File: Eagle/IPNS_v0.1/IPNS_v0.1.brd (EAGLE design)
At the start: 100 x 80 mm, 1 part, among them U1 STM8L152C4_C6TX

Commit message: Powering up microcontroller
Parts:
- added C1, C5, C6, C7, C8, C9: 1u, IPNS_Lib_v0.1:C0805
- added C2, C3: 20pF, IPNS_Lib_v0.1:C0805
- added C4: 100n, IPNS_Lib_v0.1:C0805
- added J1: (no value), IPNS_Lib_v0.1:1X04
- added Q1: 16MHz, IPNS_Lib_v0.1:HC49/S
- added R1: 0, IPNS_Lib_v0.1:R0805
- added U$1, U$2: PUSH-BUTTON, IPNS_Lib_v0.1:PUSH-BUTTON
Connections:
- removed net VDD: U1.10
- removed net VDD2: U1.39
- removed net VLCD: U1.13
- removed net VREF+: U1.12
- removed net VSS1/VSSA/VREF-: U1.9
- removed net VSS2: U1.40
- new net +3V3: C1.1, C5.1, C6.1, C7.1, J1.1, U$2.1, U1.10, U1.13, U1.39
- new net GND: C1.2, C2.1, C3.1, C4.2, C5.2, C6.2, C7.2, C8.2, C9.2, J1.3, U$1.1, U1.40, U1.9
- new net N$1: C2.2, Q1.2, U1.3
- new net N$2: R1.2, U1.4
- new net N$5: C3.2, Q1.1, R1.1
- new net RESET: C4.1, J1.4, U$1.3, U1.2
- new net ST_LINK_SWIM: J1.2, U1.1
- net VDDA: now also C8.1, C9.1, U$2.3, U1.12
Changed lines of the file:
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@@
 <attribute name="COPYRIGHT" value="Copyright (C) 2016 Accelerated Designs. All rights reserved" x="-25.4" y="6.35" size="1.778" layer="27" display="off"/>
 </element>
+<element name="C1" library="IPNS_Lib_v0.1" package="C0805" value="1u" x="-29.21" y="-3.81"/>
+<element name="Q1" library="IPNS_Lib_v0.1" package="HC49/S" value="16MHz" x="-22.86" y="-13.97">
+<attribute name="MF" value="" x="-22.86" y="-13.97" size="1.778" layer="27" display="off"/>
+<attribute name="OC_FARNELL" value="1667008" x="-22.86" y="-13.97" size="1.778" layer="27" display="off"/>
+<attribute name="OC_NEWARK" value="unknown" x="-22.86" y="-13.97" size="1.778" layer="27" display="off"/>
+<attribute name="MPN" value="" x="-22.86" y="-13.97" size="1.778" layer="27" display="off"/>
+</element>
+<element name="C2" library="IPNS_Lib_v0.1" package="C0805" value="20pF" x="-29.21" y="-24.13"/>
+<element name="C3" library="IPNS_Lib_v0.1" package="C0805" value="20pF" x="-29.21" y="-30.48"/>
+<element name="R1" library="IPNS_Lib_v0.1" package="R0805" value="0" x="-29.21" y="-36.83"/>
+<element name="J1" library="IPNS_Lib_v0.1" package="1X04" value="" x="-21.59" y="-49.53">
+<attribute name="PROD_ID" value="CONN-09696" x="-21.59" y="-49.53" size="1.778" layer="27" display="off"/>
+</element>
+<element name="U$1" library="IPNS_Lib_v0.1" package="PUSH-BUTTON" value="PUSH-BUTTON" x="-19.05" y="-68.58"/>
+<element name="C4" library="IPNS_Lib_v0.1" package="C0805" value="100n" x="-29.21" y="-81.28"/>
+<element name="C5" library="IPNS_Lib_v0.1" package="C0805" value="1u" x="-29.21" y="-87.63"/>
+<element name="C6" library="IPNS_Lib_v0.1" package="C0805" value="1u" x="-29.21" y="-93.98"/>
+<element name="C7" library="IPNS_Lib_v0.1" package="C0805" value="1u" x="-29.21" y="-100.33"/>
+<element name="C8" library="IPNS_Lib_v0.1" package="C0805" value="1u" x="-29.21" y="-106.68"/>
+<element name="C9" library="IPNS_Lib_v0.1" package="C0805" value="1u" x="-29.21" y="-113.03"/>
+<element name="U$2" library="IPNS_Lib_v0.1" package="PUSH-BUTTON" value="PUSH-BUTTON" x="-19.05" y="-125.73"/>
 </elements>
 <signals>
-<signal name="VLCD">
+<signal name="+3V3">
+<contactref element="C1" pad="1"/>
+<contactref element="U1" pad="39"/>
+<contactref element="U1" pad="10"/>
 <contactref element="U1" pad="13"/>
+<contactref element="C7" pad="1"/>
+<contactref element="C6" pad="1"/>
+<contactref element="C5" pad="1"/>
+<contactref element="J1" pad="1"/>
+<contactref element="U$2" pad="1"/>
+<wire x1="-30.16" y1="-100.33" x2="-21.59" y2="-125.73" width="0" layer="19" extent="1-1"/>
+<wire x1="-30.16" y1="-93.98" x2="-30.16" y2="-100.33" width="0" layer="19" extent="1-1"/>
+<wire x1="-30.16" y1="-87.63" x2="-30.16" y2="-93.98" width="0" layer="19" extent="1-1"/>
+<wire x1="-21.59" y1="-49.53" x2="-30.16" y2="-87.63" width="0" layer="19" extent="1-1"/>
+<wire x1="-30.16" y1="-3.81" x2="-21.59" y2="-49.53" width="0" layer="19" extent="1-1"/>
+<wire x1="-28.15000625" y1="2.1336" x2="-30.16" y2="-3.81" width="0" layer="19" extent="1-1"/>
+<wire x1="-29.6164" y1="4.599990625" x2="-28.15000625" y2="2.1336" width="0" layer="19" extent="1-1"/>
+<wire x1="-23.649990625" y1="10.5664" x2="-29.6164" y2="4.599990625" width="0" layer="19" extent="1-1"/>
 </signal>
-<signal name="VSS1/VSSA/VREF-">
+<signal name="GND">
 <contactref element="U1" pad="9"/>
+<contactref element="U1" pad="40"/>
+<contactref element="C1" pad="2"/>
+<contactref element="C2" pad="1"/>
+<contactref element="C3" pad="1"/>
+<contactref element="U$1" pad="1"/>
+<contactref element="C4" pad="2"/>
+<contactref element="C5" pad="2"/>
+<contactref element="C6" pad="2"/>
+<contactref element="C7" pad="2"/>
+<contactref element="C8" pad="2"/>
+<contactref element="C9" pad="2"/>
+<contactref element="J1" pad="3"/>
+<wire x1="-28.26" y1="-106.68" x2="-28.26" y2="-113.03" width="0" layer="19" extent="1-1"/>
+<wire x1="-28.26" y1="-100.33" x2="-28.26" y2="-106.68" width="0" layer="19" extent="1-1"/>
+<wire x1="-28.26" y1="-93.98" x2="-28.26" y2="-100.33" width="0" layer="19" extent="1-1"/>
+<wire x1="-28.26" y1="-87.63" x2="-28.26" y2="-93.98" width="0" layer="19" extent="1-1"/>
+<wire x1="-28.26" y1="-81.28" x2="-28.26" y2="-87.63" width="0" layer="19" extent="1-1"/>
+<wire x1="-21.59" y1="-68.58" x2="-28.26" y2="-81.28" width="0" layer="19" extent="1-1"/>
+<wire x1="-16.51" y1="-49.53" x2="-21.59" y2="-68.58" width="0" layer="19" extent="1-1"/>
+<wire x1="-30.16" y1="-30.48" x2="-16.51" y2="-49.53" width="0" layer="19" extent="1-1"/>
+<wire x1="-30.16" y1="-24.13" x2="-30.16" y2="-30.48" width="0" layer="19" extent="1-1"/>
+<wire x1="-28.26" y1="-3.81" x2="-30.16" y2="-24.13" width="0" layer="19" extent="1-1"/>
+<wire x1="-29.6164" y1="5.099990625" x2="-28.26" y2="-3.81" width="0" layer="19" extent="1-1"/>
+<wire x1="-24.149990625" y1="10.5664" x2="-29.6164" y2="5.099990625" width="0" layer="19" extent="1-1"/>
 </signal>
-<signal name="VSS2">
-<contactref element="U1" pad="40"/>
+<signal name="N$1">
+<contactref element="C2" pad="2"/>
+<contactref element="Q1" pad="2"/>
+<contactref element="U1" pad="3"/>
+<wire x1="-20.447" y1="-13.97" x2="-28.26" y2="-24.13" width="0" layer="19" extent="1-1"/>
+<wire x1="-29.6164" y1="8.100009375" x2="-20.447" y2="-13.97" width="0" layer="19" extent="1-1"/>
 </signal>
-<signal name="VREF+">
-<contactref element="U1" pad="12"/>
+<signal name="N$2">
+<contactref element="U1" pad="4"/>
+<contactref element="R1" pad="2"/>
+<wire x1="-29.6164" y1="7.600009375" x2="-28.26" y2="-36.83" width="0" layer="19" extent="1-1"/>
+</signal>
+<signal name="N$5">
+<contactref element="C3" pad="2"/>
+<contactref element="Q1" pad="1"/>
+<contactref element="R1" pad="1"/>
+<wire x1="-28.26" y1="-30.48" x2="-30.16" y2="-36.83" width="0" layer="19" extent="1-1"/>
+<wire x1="-25.273" y1="-13.97" x2="-28.26" y2="-30.48" width="0" layer="19" extent="1-1"/>
+</signal>
+<signal name="RESET">
+<contactref element="U$1" pad="3"/>
+<contactref element="C4" pad="1"/>
+<contactref element="U1" pad="2"/>
+<contactref element="J1" pad="4"/>
+<wire x1="-16.51" y1="-68.58" x2="-30.16" y2="-81.28" width="0" layer="19" extent="1-1"/>
+<wire x1="-13.97" y1="-49.53" x2="-16.51" y2="-68.58" width="0" layer="19" extent="1-1"/>
+<wire x1="-29.6164" y1="8.600009375" x2="-13.97" y2="-49.53" width="0" layer="19" extent="1-1"/>
+</signal>
+<signal name="ST_LINK_SWIM">
+<contactref element="U1" pad="1"/>
+<contactref element="J1" pad="2"/>
+<wire x1="-29.6164" y1="9.10000625" x2="-19.05" y2="-49.53" width="0" layer="19" extent="1-1"/>
 </signal>
 <signal name="VDDA">
+<contactref element="C8" pad="1"/>
+<contactref element="C9" pad="1"/>
 <contactref element="U1" pad="11"/>
-</signal>
-<signal name="VDD">
-<contactref element="U1" pad="10"/>
-</signal>
-<signal name="VDD2">
-<contactref element="U1" pad="39"/>
+<contactref element="U1" pad="12"/>
+<contactref element="U$2" pad="3"/>
+<wire x1="-30.16" y1="-106.68" x2="-30.16" y2="-113.03" width="0" layer="19" extent="1-1"/>
+<wire x1="-16.51" y1="-125.73" x2="-30.16" y2="-113.03" width="0" layer="19" extent="1-1"/>
+<wire x1="-29.6164" y1="3.59999375" x2="-30.16" y2="-106.68" width="0" layer="19" extent="1-1"/>
+<wire x1="-29.6164" y1="4.099990625" x2="-29.6164" y2="3.59999375" width="0" layer="19" extent="1-1"/>
 </signal>
 </signals>

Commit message: Microcontroller setup possibly finished with minor unknowns
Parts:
- added C10, C11: 7pF, IPNS_Lib_v0.1:C0805
- added C12: (no value), IPNS_Lib_v0.1:C0805
- added J2: (no value), IPNS_Lib_v0.1:1X04
- added LED1: RED, led:CHIP-LED0805
- added LED2: GREEN, led:CHIP-LED0805
- added LED3: BLUE, led:CHIP-LED0805
- added Q2: 32.768 kHz, IPNS_Lib_v0.1:TC26H
- added R2: 0, IPNS_Lib_v0.1:R0805
- added R3, R4, R5, R6, R7: (no value), IPNS_Lib_v0.1:R0805
- C6, C7, C9: value 1u -> 100n
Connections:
- new net DAC: U1.32
- new net N$11: LED1.A, R3.1
- new net N$12: LED2.A, R4.1
- new net N$13: LED3.A, R5.1
- new net N$14: R3.2, U1.48
- new net N$15: R4.2, U1.47
- new net N$16: R5.2, U1.19
- new net N$3: C11.2, Q2.1, R2.1
- new net N$4: C5.1, C6.1, C7.1, U$2.1
- new net N$6: C10.2, Q2.2, U1.44
- new net N$8: R2.2, U1.45
- new net PULSE: U1.22
- new net SCL: J2.3, R6.1, U1.38
- new net SDA: J2.4, R7.1, U1.37
- net +3V3: now also C12.2, J2.2, R6.2, R7.2; no longer C5.1, C6.1, C7.1, U$2.1
- net GND: now also C10.1, C11.1, C12.1, J2.1, LED1.C, LED2.C, LED3.C
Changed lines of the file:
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@@
 <setting verticaltext="up"/>
 </settings>
-<grid distance="0.05" unitdist="inch" unit="inch" style="lines" multiple="1" display="no" altdistance="0.025" altunitdist="inch" altunit="inch"/>
+<grid distance="0.05" unitdist="inch" unit="inch" style="lines" multiple="1" display="yes" altdistance="0.025" altunitdist="inch" altunit="inch"/>
 <layers>
 <layer number="1" name="Top" color="4" fill="1" visible="yes" active="yes"/>
@@
 <element name="C4" library="IPNS_Lib_v0.1" package="C0805" value="100n" x="-29.21" y="-81.28"/>
 <element name="C5" library="IPNS_Lib_v0.1" package="C0805" value="1u" x="-29.21" y="-87.63"/>
-<element name="C6" library="IPNS_Lib_v0.1" package="C0805" value="1u" x="-29.21" y="-93.98"/>
-<element name="C7" library="IPNS_Lib_v0.1" package="C0805" value="1u" x="-29.21" y="-100.33"/>
+<element name="C6" library="IPNS_Lib_v0.1" package="C0805" value="100n" x="-29.21" y="-93.98"/>
+<element name="C7" library="IPNS_Lib_v0.1" package="C0805" value="100n" x="-29.21" y="-100.33"/>
 <element name="C8" library="IPNS_Lib_v0.1" package="C0805" value="1u" x="-29.21" y="-106.68"/>
-<element name="C9" library="IPNS_Lib_v0.1" package="C0805" value="1u" x="-29.21" y="-113.03"/>
+<element name="C9" library="IPNS_Lib_v0.1" package="C0805" value="100n" x="-29.21" y="-113.03"/>
 <element name="U$2" library="IPNS_Lib_v0.1" package="PUSH-BUTTON" value="PUSH-BUTTON" x="-19.05" y="-125.73"/>
+<element name="Q2" library="IPNS_Lib_v0.1" package="TC26H" value="32.768 kHz" x="-21.59" y="-144.78">
+<attribute name="MF" value="" x="-21.59" y="-144.78" size="1.778" layer="27" display="off"/>
+<attribute name="OC_FARNELL" value="unknown" x="-21.59" y="-144.78" size="1.778" layer="27" display="off"/>
+<attribute name="OC_NEWARK" value="unknown" x="-21.59" y="-144.78" size="1.778" layer="27" display="off"/>
+<attribute name="MPN" value="" x="-21.59" y="-144.78" size="1.778" layer="27" display="off"/>
+</element>
+<element name="C10" library="IPNS_Lib_v0.1" package="C0805" value="7pF" x="-29.21" y="-156.21"/>
+<element name="C11" library="IPNS_Lib_v0.1" package="C0805" value="7pF" x="-29.21" y="-162.56"/>
+<element name="R2" library="IPNS_Lib_v0.1" package="R0805" value="0" x="-29.21" y="-168.91"/>
+<element name="R3" library="IPNS_Lib_v0.1" package="R0805" value="" x="-29.21" y="-175.26"/>
+<element name="R4" library="IPNS_Lib_v0.1" package="R0805" value="" x="-29.21" y="-181.61"/>
+<element name="R5" library="IPNS_Lib_v0.1" package="R0805" value="" x="-29.21" y="-187.96"/>
+<element name="LED1" library="led" package="CHIP-LED0805" value="RED" x="-35.56" y="-187.96"/>
+<element name="LED2" library="led" package="CHIP-LED0805" value="GREEN" x="-41.91" y="-187.96"/>
+<element name="LED3" library="led" package="CHIP-LED0805" value="BLUE" x="-48.26" y="-187.96"/>
+<element name="J2" library="IPNS_Lib_v0.1" package="1X04" value="" x="-40.64" y="-200.66">
+<attribute name="PROD_ID" value="CONN-09696" x="-40.64" y="-200.66" size="1.778" layer="27" display="off"/>
+</element>
+<element name="C12" library="IPNS_Lib_v0.1" package="C0805" value="" x="-48.26" y="-213.36"/>
+<element name="R6" library="IPNS_Lib_v0.1" package="R0805" value="" x="-48.26" y="-219.71"/>
+<element name="R7" library="IPNS_Lib_v0.1" package="R0805" value="" x="-48.26" y="-226.06"/>
 </elements>
 <signals>
@@
 <contactref element="U1" pad="10"/>
 <contactref element="U1" pad="13"/>
-<contactref element="C7" pad="1"/>
-<contactref element="C6" pad="1"/>
-<contactref element="C5" pad="1"/>
 <contactref element="J1" pad="1"/>
-<contactref element="U$2" pad="1"/>
-<wire x1="-30.16" y1="-100.33" x2="-21.59" y2="-125.73" width="0" layer="19" extent="1-1"/>
-<wire x1="-30.16" y1="-93.98" x2="-30.16" y2="-100.33" width="0" layer="19" extent="1-1"/>
-<wire x1="-30.16" y1="-87.63" x2="-30.16" y2="-93.98" width="0" layer="19" extent="1-1"/>
-<wire x1="-21.59" y1="-49.53" x2="-30.16" y2="-87.63" width="0" layer="19" extent="1-1"/>
+<contactref element="J2" pad="2"/>
+<contactref element="C12" pad="2"/>
+<contactref element="R6" pad="2"/>
+<contactref element="R7" pad="2"/>
+<wire x1="-47.31" y1="-213.36" x2="-38.1" y2="-200.66" width="0" layer="19" extent="1-1"/>
+<wire x1="-47.31" y1="-219.71" x2="-47.31" y2="-213.36" width="0" layer="19" extent="1-1"/>
+<wire x1="-47.31" y1="-226.06" x2="-47.31" y2="-219.71" width="0" layer="19" extent="1-1"/>
+<wire x1="-21.59" y1="-49.53" x2="-38.1" y2="-200.66" width="0" layer="19" extent="1-1"/>
 <wire x1="-30.16" y1="-3.81" x2="-21.59" y2="-49.53" width="0" layer="19" extent="1-1"/>
 <wire x1="-28.15000625" y1="2.1336" x2="-30.16" y2="-3.81" width="0" layer="19" extent="1-1"/>
@@
 <contactref element="C9" pad="2"/>
 <contactref element="J1" pad="3"/>
+<contactref element="C10" pad="1"/>
+<contactref element="C11" pad="1"/>
+<contactref element="LED1" pad="C"/>
+<contactref element="LED2" pad="C"/>
+<contactref element="LED3" pad="C"/>
+<contactref element="J2" pad="1"/>
+<contactref element="C12" pad="1"/>
+<wire x1="-41.91" y1="-186.91" x2="-40.64" y2="-200.66" width="0" layer="19" extent="1-1"/>
+<wire x1="-48.26" y1="-186.91" x2="-41.91" y2="-186.91" width="0" layer="19" extent="1-1"/>
+<wire x1="-35.56" y1="-186.91" x2="-41.91" y2="-186.91" width="0" layer="19" extent="1-1"/>
+<wire x1="-49.21" y1="-213.36" x2="-40.64" y2="-200.66" width="0" layer="19" extent="1-1"/>
+<wire x1="-30.16" y1="-162.56" x2="-35.56" y2="-186.91" width="0" layer="19" extent="1-1"/>
+<wire x1="-30.16" y1="-156.21" x2="-30.16" y2="-162.56" width="0" layer="19" extent="1-1"/>
+<wire x1="-28.26" y1="-113.03" x2="-30.16" y2="-156.21" width="0" layer="19" extent="1-1"/>
 <wire x1="-28.26" y1="-106.68" x2="-28.26" y2="-113.03" width="0" layer="19" extent="1-1"/>
 <wire x1="-28.26" y1="-100.33" x2="-28.26" y2="-106.68" width="0" layer="19" extent="1-1"/>
@@
 <wire x1="-29.6164" y1="4.099990625" x2="-29.6164" y2="3.59999375" width="0" layer="19" extent="1-1"/>
 </signal>
+<signal name="N$4">
+<contactref element="C5" pad="1"/>
+<contactref element="C6" pad="1"/>
+<contactref element="C7" pad="1"/>
+<contactref element="U$2" pad="1"/>
+<wire x1="-30.16" y1="-100.33" x2="-21.59" y2="-125.73" width="0" layer="19" extent="1-1"/>
+<wire x1="-30.16" y1="-93.98" x2="-30.16" y2="-100.33" width="0" layer="19" extent="1-1"/>
+<wire x1="-30.16" y1="-87.63" x2="-30.16" y2="-93.98" width="0" layer="19" extent="1-1"/>
+</signal>
+<signal name="N$3">
+<contactref element="R2" pad="1"/>
+<contactref element="C11" pad="2"/>
+<contactref element="Q2" pad="1"/>
+<wire x1="-28.26" y1="-162.56" x2="-30.16" y2="-168.91" width="0" layer="19" extent="1-1"/>
+<wire x1="-22.86" y1="-144.78" x2="-28.26" y2="-162.56" width="0" layer="19" extent="1-1"/>
+</signal>
+<signal name="N$6">
+<contactref element="Q2" pad="2"/>
+<contactref element="C10" pad="2"/>
+<contactref element="U1" pad="44"/>
+<wire x1="-20.32" y1="-144.78" x2="-28.26" y2="-156.21" width="0" layer="19" extent="1-1"/>
+<wire x1="-26.1500125" y1="10.5664" x2="-20.32" y2="-144.78" width="0" layer="19" extent="1-1"/>
+</signal>
+<signal name="N$8">
+<contactref element="U1" pad="45"/>
+<contactref element="R2" pad="2"/>
+<wire x1="-26.650009375" y1="10.5664" x2="-28.26" y2="-168.91" width="0" layer="19" extent="1-1"/>
+</signal>
+<signal name="N$11">
+<contactref element="LED1" pad="A"/>
+<contactref element="R3" pad="1"/>
+<wire x1="-30.16" y1="-175.26" x2="-35.56" y2="-189.01" width="0" layer="19" extent="1-1"/>
+</signal>
+<signal name="N$12">
+<contactref element="LED2" pad="A"/>
+<contactref element="R4" pad="1"/>
+<wire x1="-30.16" y1="-181.61" x2="-41.91" y2="-189.01" width="0" layer="19" extent="1-1"/>
+</signal>
+<signal name="N$13">
+<contactref element="LED3" pad="A"/>
+<contactref element="R5" pad="1"/>
+<wire x1="-30.16" y1="-187.96" x2="-48.26" y2="-189.01" width="0" layer="19" extent="1-1"/>
+</signal>
+<signal name="N$14">
+<contactref element="R3" pad="2"/>
+<contactref element="U1" pad="48"/>
+<wire x1="-28.15000625" y1="10.5664" x2="-28.26" y2="-175.26" width="0" layer="19" extent="1-1"/>
+</signal>
+<signal name="N$15">
+<contactref element="R4" pad="2"/>
+<contactref element="U1" pad="47"/>
+<wire x1="-27.650009375" y1="10.5664" x2="-28.26" y2="-181.61" width="0" layer="19" extent="1-1"/>
+</signal>
+<signal name="N$16">
+<contactref element="R5" pad="2"/>
+<contactref element="U1" pad="19"/>
+<wire x1="-25.1500125" y1="2.1336" x2="-28.26" y2="-187.96" width="0" layer="19" extent="1-1"/>
+</signal>
+<signal name="DAC">
+<contactref element="U1" pad="32"/>
+</signal>
+<signal name="PULSE">
+<contactref element="U1" pad="22"/>
+</signal>
+<signal name="SCL">
+<contactref element="U1" pad="38"/>
+<contactref element="J2" pad="3"/>
+<contactref element="R6" pad="1"/>
+<wire x1="-49.21" y1="-219.71" x2="-35.56" y2="-200.66" width="0" layer="19" extent="1-1"/>
+<wire x1="-23.149990625" y1="10.5664" x2="-35.56" y2="-200.66" width="0" layer="19" extent="1-1"/>
+</signal>
+<signal name="SDA">
+<contactref element="U1" pad="37"/>
+<contactref element="J2" pad="4"/>
+<contactref element="R7" pad="1"/>
+<wire x1="-49.21" y1="-226.06" x2="-33.02" y2="-200.66" width="0" layer="19" extent="1-1"/>
+<wire x1="-22.64999375" y1="10.5664" x2="-33.02" y2="-200.66" width="0" layer="19" extent="1-1"/>
+</signal>
 </signals>

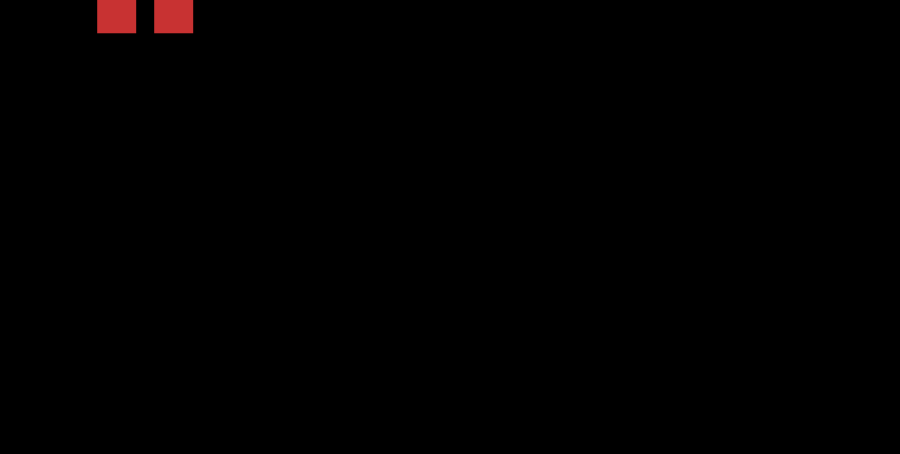
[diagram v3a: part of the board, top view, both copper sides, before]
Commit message: Various connectors implemented: SWIM , battery supply board, and NFC memory connector
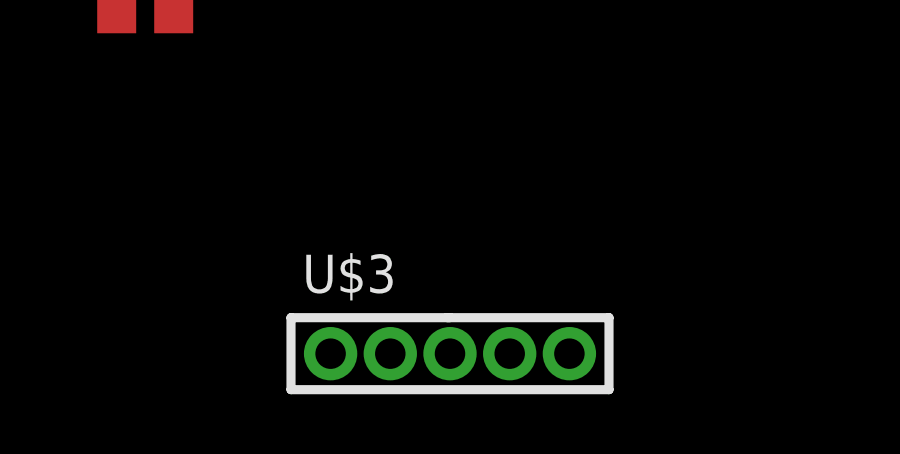
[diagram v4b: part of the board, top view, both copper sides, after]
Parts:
- added U$3: SLIDE_SWITCH, IPNS_Lib_v0.1:SLIDE_SWITCH
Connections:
- new net OFF: U$3.2
- new net VBATT: U$3.3
- net +3V3: now also U$3.4
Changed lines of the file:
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@@
 <element name="R6" library="IPNS_Lib_v0.1" package="R0805" value="" x="-48.26" y="-219.71"/>
 <element name="R7" library="IPNS_Lib_v0.1" package="R0805" value="" x="-48.26" y="-226.06"/>
+<element name="U$3" library="IPNS_Lib_v0.1" package="SLIDE_SWITCH" value="SLIDE_SWITCH" x="-38.1" y="-237.49"/>
 </elements>
 <signals>
@@
 <contactref element="R6" pad="2"/>
 <contactref element="R7" pad="2"/>
+<contactref element="U$3" pad="4"/>
 <wire x1="-47.31" y1="-213.36" x2="-38.1" y2="-200.66" width="0" layer="19" extent="1-1"/>
 <wire x1="-47.31" y1="-219.71" x2="-47.31" y2="-213.36" width="0" layer="19" extent="1-1"/>
 <wire x1="-47.31" y1="-226.06" x2="-47.31" y2="-219.71" width="0" layer="19" extent="1-1"/>
+<wire x1="-36.11" y1="-237.49" x2="-47.31" y2="-226.06" width="0" layer="19" extent="1-1"/>
 <wire x1="-21.59" y1="-49.53" x2="-38.1" y2="-200.66" width="0" layer="19" extent="1-1"/>
 <wire x1="-30.16" y1="-3.81" x2="-21.59" y2="-49.53" width="0" layer="19" extent="1-1"/>
@@
 <wire x1="-22.64999375" y1="10.5664" x2="-33.02" y2="-200.66" width="0" layer="19" extent="1-1"/>
 </signal>
+<signal name="VBATT">
+<contactref element="U$3" pad="3"/>
+</signal>
+<signal name="OFF">
+<contactref element="U$3" pad="2"/>
+</signal>
 </signals>

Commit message: The physical board started
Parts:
- moved J2 285.2 mm to (69.8, 62.2)
- moved R7 277.1 mm to (90.2, 14.0)
- moved R6 265.0 mm to (81.3, 11.4)
- moved U$3 258.3 mm to (47.0, 6.35)
- moved C12 254.6 mm to (73.7, 10.2)
- moved R2 232.3 mm to (53.3, 48.3)
- moved C10 231.7 mm to (21.6, 69.8)
- moved C11 227.3 mm to (41.9, 53.3)
- moved LED3 202.8 mm to (14.0, 5.08), turned to 180 degrees
- moved R5 201.5 mm to (14.0, 8.89), turned to 90 degrees
- moved LED2 199.9 mm to (10.2, 5.08), turned to 180 degrees
- moved LED1 197.5 mm to (6.35, 5.08), turned to 180 degrees
- moved R4 194.5 mm to (10.2, 8.89), turned to 90 degrees
- moved R3 187.6 mm to (6.35, 8.89), turned to 90 degrees
- moved Q2 179.9 mm to (24.1, 29.2)
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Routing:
- added copper zone on layer 1, net GND
